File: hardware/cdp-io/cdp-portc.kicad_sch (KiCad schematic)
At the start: 5 parts, among them U1 74LS573, U2 74LS573, U7 74LS00

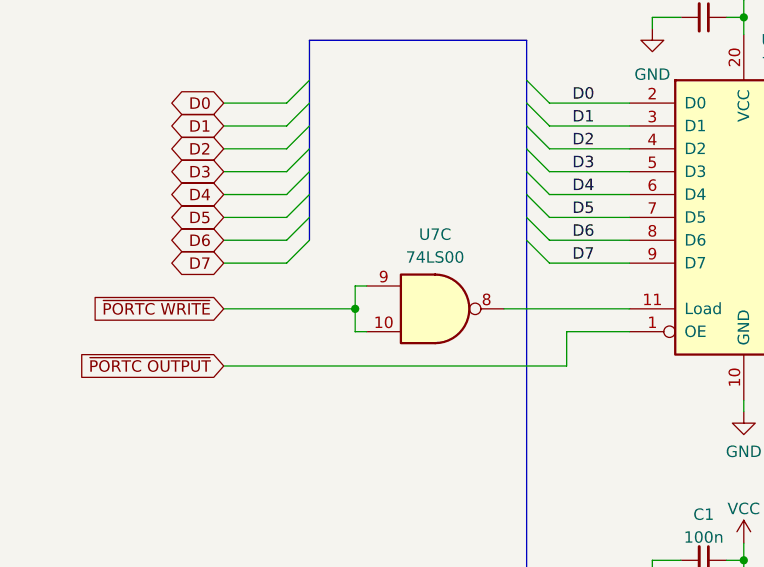
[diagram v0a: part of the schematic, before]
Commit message: The controller is finished. U7 is changed to a hex inverter.
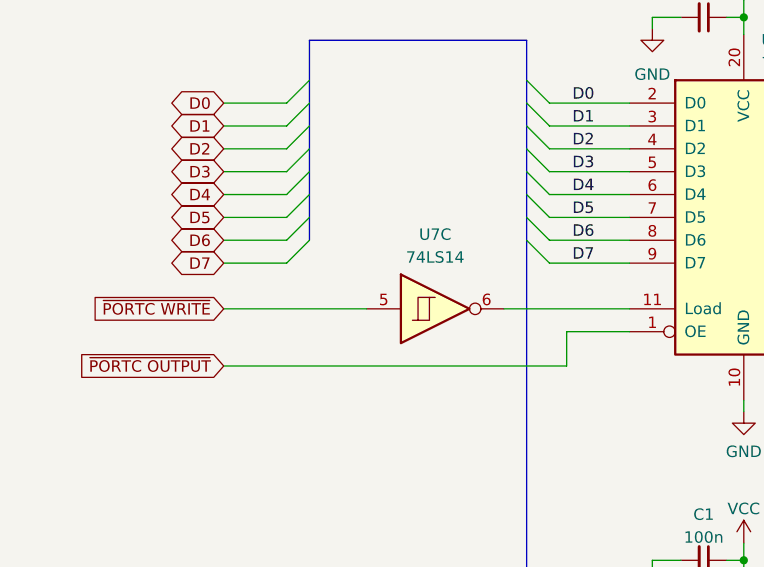
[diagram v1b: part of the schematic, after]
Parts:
- removed U7: 74LS00, symbol 74xx:74LS00
- added U7: 74LS14, symbol 74xx:74LS14
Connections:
- net ~{PORTC WRITE}: now also U7.5
- net at U1.11 (Load): now also U7.6
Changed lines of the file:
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@@
   (junction (at 155.575 33.02) (diameter 0) (color 0 0 0 0)
   )
-  (junction (at 112.395 65.405) (diameter 0) (color 0 0 0 0)
-  )
   (bus_entry (at 181.61 118.11) (size -2.54 2.54)
     (stroke (width 0) (type default))
@@
     (stroke (width 0) (type default))
   )
-  (wire (pts (xy 113.665 62.865) (xy 112.395 62.865))
-    (stroke (width 0) (type default))
-  )
   (wire (pts (xy 133.985 102.87) (xy 142.875 102.87))
     (stroke (width 0) (type default))
@@
     (stroke (width 0) (type default))
   )
-  (wire (pts (xy 112.395 65.405) (xy 112.395 67.945))
-    (stroke (width 0) (type default))
-  )
   (wire (pts (xy 145.415 94.615) (xy 145.415 93.345))
     (stroke (width 0) (type default))
@@
     (stroke (width 0) (type default))
   )
-  (wire (pts (xy 112.395 67.945) (xy 113.665 67.945))
-    (stroke (width 0) (type default))
-  )
   (wire (pts (xy 208.915 60.325) (xy 216.535 60.325))
     (stroke (width 0) (type default))
@@
     (stroke (width 0) (type default))
   )
-  (wire (pts (xy 97.79 65.405) (xy 112.395 65.405))
-    (stroke (width 0) (type default))
-  )
   (bus (pts (xy 206.375 47.625) (xy 206.375 50.165))
     (stroke (width 0) (type default))
@@
     (stroke (width 0) (type default))
   )
+  (wire (pts (xy 97.79 65.405) (xy 113.665 65.405))
+    (stroke (width 0) (type default))
+  )
   (bus (pts (xy 131.445 50.165) (xy 131.445 47.625))
     (stroke (width 0) (type default))
@@
   )
   (wire (pts (xy 145.415 34.29) (xy 145.415 33.02))
-    (stroke (width 0) (type default))
-  )
-  (wire (pts (xy 112.395 62.865) (xy 112.395 65.405))
     (stroke (width 0) (type default))
   )
@@
         (path "/479e9a3e-8705-41df-8009-7e8503809f49/03dab4a8-d44b-4cf8-b119-6efcff8953b4"
           (reference "#PWR018") (unit 1)
+        )
+      )
+    )
+  )
+  (symbol (lib_id "74xx:74LS14") (at 121.285 65.405 0) (unit 3)
+    (in_bom yes) (on_board yes) (dnp no) (fields_autoplaced)
+    (property "Reference" "U7" (at 121.285 57.15 0)
+      (effects (font (size 1.27 1.27)))
+    )
+    (property "Value" "74LS14" (at 121.285 59.69 0)
+      (effects (font (size 1.27 1.27)))
+    )
+    (property "Footprint" "" (at 121.285 65.405 0)
+      (effects (font (size 1.27 1.27)) hide)
+    )
+    (property "Datasheet" "http://www.ti.com/lit/gpn/sn74LS14" (at 121.285 65.405 0)
+      (effects (font (size 1.27 1.27)) hide)
+    )
+    (pin "1")
+    (pin "2")
+    (pin "3")
+    (pin "4")
+    (pin "5")
+    (pin "6")
+    (pin "8")
+    (pin "9")
+    (pin "10")
+    (pin "11")
+    (pin "12")
+    (pin "13")
+    (pin "14")
+    (pin "7")
+    (instances
+      (project "cdp-io"
+        (path "/479e9a3e-8705-41df-8009-7e8503809f49/fc5dd19a-450f-4ce7-af21-025e7154e993"
+          (reference "U7") (unit 3)
+        )
+        (path "/479e9a3e-8705-41df-8009-7e8503809f49/03dab4a8-d44b-4cf8-b119-6efcff8953b4"
+          (reference "U7") (unit 3)
         )
       )
@@
         )
       )
-    )
-  )
-  (symbol (lib_id "74xx:74LS00") (at 121.285 65.405 0) (unit 3)
-    (in_bom yes) (on_board yes) (dnp no) (fields_autoplaced)
-    (property "Reference" "U7" (at 121.2767 57.15 0)
-      (effects (font (size 1.27 1.27)))
-    )
-    (property "Value" "74LS00" (at 121.2767 59.69 0)
-      (effects (font (size 1.27 1.27)))
-    )
-    (property "Footprint" "" (at 121.285 65.405 0)
-      (effects (font (size 1.27 1.27)) hide)
-    )
-    (property "Datasheet" "http://www.ti.com/lit/gpn/sn74ls00" (at 121.285 65.405 0)
-      (effects (font (size 1.27 1.27)) hide)
-    )
-    (pin "1")
-    (pin "2")
-    (pin "3")
-    (pin "4")
-    (pin "5")
-    (pin "6")
-    (pin "10")
-    (pin "8")
-    (pin "9")
-    (pin "11")
-    (pin "12")
-    (pin "13")
-    (pin "14")
-    (pin "7")
-    (instances
-      (project "cdp-io"
-        (path "/479e9a3e-8705-41df-8009-7e8503809f49/03dab4a8-d44b-4cf8-b119-6efcff8953b4"
-          (reference "U7") (unit 3)
-        )
-      )

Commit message: Changed the layout a bit, started to work on the PCB.
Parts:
- U7: footprint (none) -> Package_DIP:DIP-14_W7.62mm_Socket
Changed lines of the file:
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@@
       (effects (font (size 1.27 1.27)))
     )
-    (property "Footprint" "" (at 121.285 65.405 0)
+    (property "Footprint" "Package_DIP:DIP-14_W7.62mm_Socket" (at 121.285 65.405 0)
       (effects (font (size 1.27 1.27)) hide)
     )

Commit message: Changed the schematic a bit.
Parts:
- removed U7: 74LS14, Package_DIP:DIP-14_W7.62mm_Socket, symbol 74xx:74LS14
- added U7: 74LS14, Package_DIP:DIP-14_W7.62mm_Socket, symbol 74xx:74LS14
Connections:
- net ~{PORTC WRITE}: now also U7.9
- net at U1.11 (Load): now also U7.8

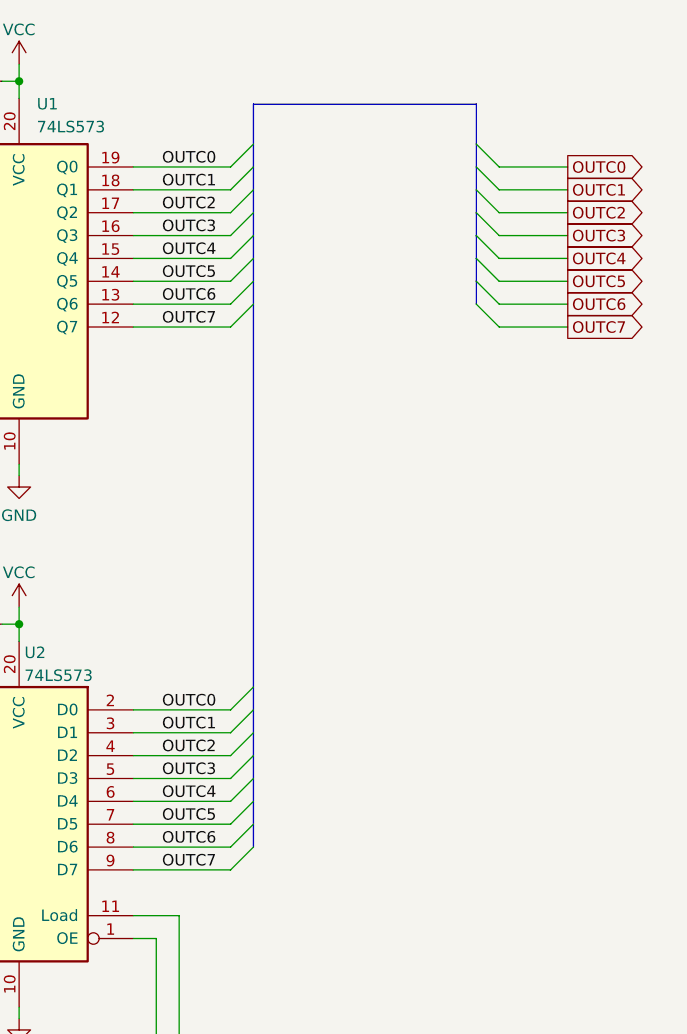
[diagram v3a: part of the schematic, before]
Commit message: Renamed a few net, and changed the schematic a bit. The PCB is ready!
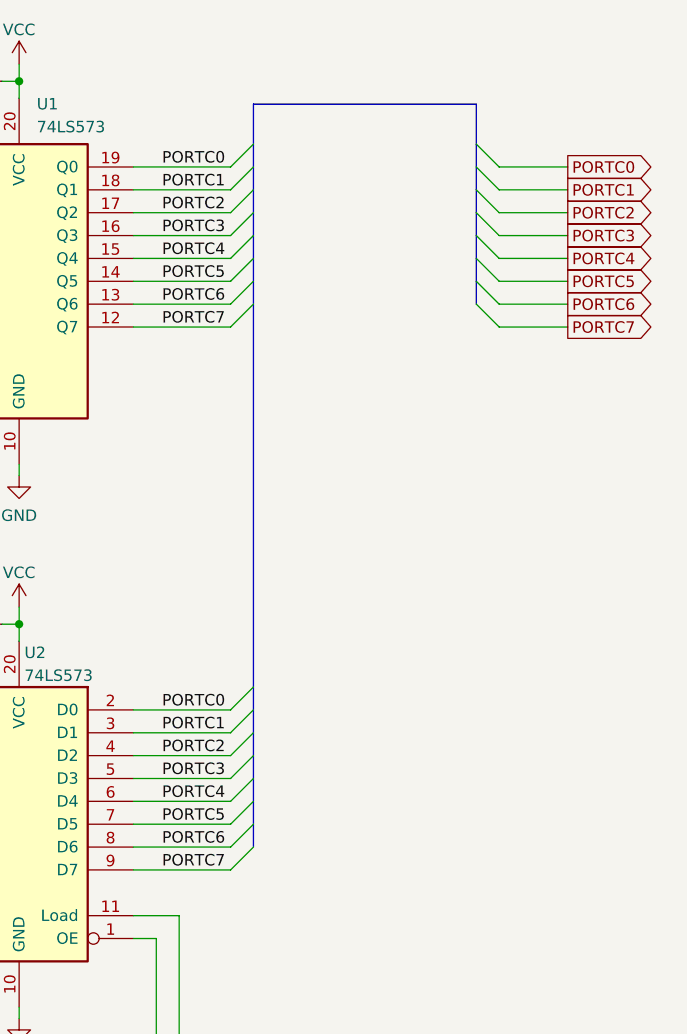
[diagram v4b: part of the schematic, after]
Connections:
- net OUTC0 renamed PORTC0
- net OUTC1 renamed PORTC1
- net OUTC2 renamed PORTC2
- net OUTC3 renamed PORTC3
- net OUTC4 renamed PORTC4
- net OUTC5 renamed PORTC5
- net OUTC6 renamed PORTC6
- net OUTC7 renamed PORTC7
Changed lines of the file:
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@@
     (effects (font (size 1.27 1.27)) (justify left bottom))
   )
-  (label "OUTC7" (at 171.45 120.65 0) (fields_autoplaced)
+  (label "PORTC7" (at 171.45 120.65 0) (fields_autoplaced)
     (effects (font (size 1.27 1.27)) (justify left bottom))
   )
-  (label "OUTC2" (at 171.45 107.95 0) (fields_autoplaced)
+  (label "PORTC2" (at 171.45 107.95 0) (fields_autoplaced)
     (effects (font (size 1.27 1.27)) (justify left bottom))
   )
-  (label "OUTC1" (at 171.45 105.41 0) (fields_autoplaced)
+  (label "PORTC1" (at 171.45 105.41 0) (fields_autoplaced)
     (effects (font (size 1.27 1.27)) (justify left bottom))
   )
@@
     (effects (font (size 1.27 1.27)) (justify left bottom))
   )
-  (label "OUTC5" (at 171.45 115.57 0) (fields_autoplaced)
+  (label "PORTC5" (at 171.45 115.57 0) (fields_autoplaced)
     (effects (font (size 1.27 1.27)) (justify left bottom))
   )
-  (label "OUTC6" (at 171.45 57.785 0) (fields_autoplaced)
+  (label "PORTC6" (at 171.45 57.785 0) (fields_autoplaced)
     (effects (font (size 1.27 1.27)) (justify left bottom))
   )
-  (label "OUTC3" (at 171.45 50.165 0) (fields_autoplaced)
+  (label "PORTC3" (at 171.45 50.165 0) (fields_autoplaced)
     (effects (font (size 1.27 1.27)) (justify left bottom))
   )
-  (label "OUTC0" (at 171.45 102.87 0) (fields_autoplaced)
+  (label "PORTC0" (at 171.45 102.87 0) (fields_autoplaced)
     (effects (font (size 1.27 1.27)) (justify left bottom))
   )
-  (label "OUTC7" (at 171.45 60.325 0) (fields_autoplaced)
+  (label "PORTC7" (at 171.45 60.325 0) (fields_autoplaced)
     (effects (font (size 1.27 1.27)) (justify left bottom))
   )
@@
     (effects (font (size 1.27 1.27)) (justify left bottom))
   )
-  (label "OUTC5" (at 171.45 55.245 0) (fields_autoplaced)
+  (label "PORTC5" (at 171.45 55.245 0) (fields_autoplaced)
     (effects (font (size 1.27 1.27)) (justify left bottom))
   )
-  (label "OUTC3" (at 171.45 110.49 0) (fields_autoplaced)
+  (label "PORTC3" (at 171.45 110.49 0) (fields_autoplaced)
     (effects (font (size 1.27 1.27)) (justify left bottom))
   )
-  (label "OUTC4" (at 171.45 52.705 0) (fields_autoplaced)
+  (label "PORTC4" (at 171.45 52.705 0) (fields_autoplaced)
     (effects (font (size 1.27 1.27)) (justify left bottom))
   )
-  (label "OUTC6" (at 171.45 118.11 0) (fields_autoplaced)
+  (label "PORTC6" (at 171.45 118.11 0) (fields_autoplaced)
     (effects (font (size 1.27 1.27)) (justify left bottom))
   )
-  (label "OUTC1" (at 171.45 45.085 0) (fields_autoplaced)
+  (label "PORTC1" (at 171.45 45.085 0) (fields_autoplaced)
     (effects (font (size 1.27 1.27)) (justify left bottom))
   )
@@
     (effects (font (size 1.27 1.27)) (justify left bottom))
   )
-  (label "OUTC0" (at 171.45 42.545 0) (fields_autoplaced)
+  (label "PORTC0" (at 171.45 42.545 0) (fields_autoplaced)
     (effects (font (size 1.27 1.27)) (justify left bottom))
   )
@@
     (effects (font (size 1.27 1.27)) (justify left bottom))
   )
-  (label "OUTC2" (at 171.45 47.625 0) (fields_autoplaced)
+  (label "PORTC2" (at 171.45 47.625 0) (fields_autoplaced)
     (effects (font (size 1.27 1.27)) (justify left bottom))
   )
@@
     (effects (font (size 1.27 1.27)) (justify left bottom))
   )
-  (label "OUTC4" (at 171.45 113.03 0) (fields_autoplaced)
+  (label "PORTC4" (at 171.45 113.03 0) (fields_autoplaced)
     (effects (font (size 1.27 1.27)) (justify left bottom))
   )
@@
     )
   )
-  (global_label "OUTC1" (shape output) (at 216.535 45.085 0) (fields_autoplaced)
+  (global_label "PORTC1" (shape output) (at 216.535 45.085 0) (fields_autoplaced)
     (effects (font (size 1.27 1.27)) (justify left))
-    (property "Intersheetrefs" "${INTERSHEET_REFS}" (at 225.5489 45.085 0)
+    (property "Intersheetrefs" "${INTERSHEET_REFS}" (at 226.7584 45.085 0)
       (effects (font (size 1.27 1.27)) (justify left) hide)
     )
   )
-  (global_label "OUTC2" (shape output) (at 216.535 47.625 0) (fields_autoplaced)
+  (global_label "PORTC2" (shape output) (at 216.535 47.625 0) (fields_autoplaced)
     (effects (font (size 1.27 1.27)) (justify left))
-    (property "Intersheetrefs" "${INTERSHEET_REFS}" (at 225.5489 47.625 0)
+    (property "Intersheetrefs" "${INTERSHEET_REFS}" (at 226.7584 47.625 0)
       (effects (font (size 1.27 1.27)) (justify left) hide)
     )
   )
-  (global_label "OUTC0" (shape output) (at 216.535 42.545 0) (fields_autoplaced)
+  (global_label "PORTC0" (shape output) (at 216.535 42.545 0) (fields_autoplaced)
     (effects (font (size 1.27 1.27)) (justify left))
-    (property "Intersheetrefs" "${INTERSHEET_REFS}" (at 225.5489 42.545 0)
+    (property "Intersheetrefs" "${INTERSHEET_REFS}" (at 226.7584 42.545 0)
       (effects (font (size 1.27 1.27)) (justify left) hide)
     )
   )
-  (global_label "OUTC7" (shape output) (at 216.535 60.325 0) (fields_autoplaced)
+  (global_label "PORTC7" (shape output) (at 216.535 60.325 0) (fields_autoplaced)
     (effects (font (size 1.27 1.27)) (justify left))
-    (property "Intersheetrefs" "${INTERSHEET_REFS}" (at 225.5489 60.325 0)
+    (property "Intersheetrefs" "${INTERSHEET_REFS}" (at 226.7584 60.325 0)
       (effects (font (size 1.27 1.27)) (justify left) hide)
     )
   )
-  (global_label "OUTC4" (shape output) (at 216.535 52.705 0) (fields_autoplaced)
+  (global_label "PORTC4" (shape output) (at 216.535 52.705 0) (fields_autoplaced)
     (effects (font (size 1.27 1.27)) (justify left))
-    (property "Intersheetrefs" "${INTERSHEET_REFS}" (at 225.5489 52.705 0)
+    (property "Intersheetrefs" "${INTERSHEET_REFS}" (at 226.7584 52.705 0)
       (effects (font (size 1.27 1.27)) (justify left) hide)
     )
@@
     )
   )
-  (global_label "OUTC5" (shape output) (at 216.535 55.245 0) (fields_autoplaced)
+  (global_label "PORTC5" (shape output) (at 216.535 55.245 0) (fields_autoplaced)
     (effects (font (size 1.27 1.27)) (justify left))
-    (property "Intersheetrefs" "${INTERSHEET_REFS}" (at 225.5489 55.245 0)
+    (property "Intersheetrefs" "${INTERSHEET_REFS}" (at 226.7584 55.245 0)
       (effects (font (size 1.27 1.27)) (justify left) hide)
     )
@@
     )
   )
-  (global_label "OUTC3" (shape output) (at 216.535 50.165 0) (fields_autoplaced)
+  (global_label "PORTC3" (shape output) (at 216.535 50.165 0) (fields_autoplaced)
     (effects (font (size 1.27 1.27)) (justify left))
-    (property "Intersheetrefs" "${INTERSHEET_REFS}" (at 225.5489 50.165 0)
+    (property "Intersheetrefs" "${INTERSHEET_REFS}" (at 226.7584 50.165 0)
       (effects (font (size 1.27 1.27)) (justify left) hide)
     )
   )
-  (global_label "OUTC6" (shape output) (at 216.535 57.785 0) (fields_autoplaced)
+  (global_label "PORTC6" (shape output) (at 216.535 57.785 0) (fields_autoplaced)
     (effects (font (size 1.27 1.27)) (justify left))
-    (property "Intersheetrefs" "${INTERSHEET_REFS}" (at 225.5489 57.785 0)
+    (property "Intersheetrefs" "${INTERSHEET_REFS}" (at 226.7584 57.785 0)
       (effects (font (size 1.27 1.27)) (justify left) hide)
     )

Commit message: The final version of the IO board. Gerber files added.
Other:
- company: (none) -> ZLED
- title: (none) -> Port C
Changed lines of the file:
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@@
 (kicad_sch (version 20230121) (generator eeschema)
   (paper "A4")
+  (title_block
+    (title "Port C")
+    (date "2023-07-06")
+    (rev "1")
+    (company "ZLED")
+  )
   (junction (at 155.575 93.345) (diameter 0) (color 0 0 0 0)
   )

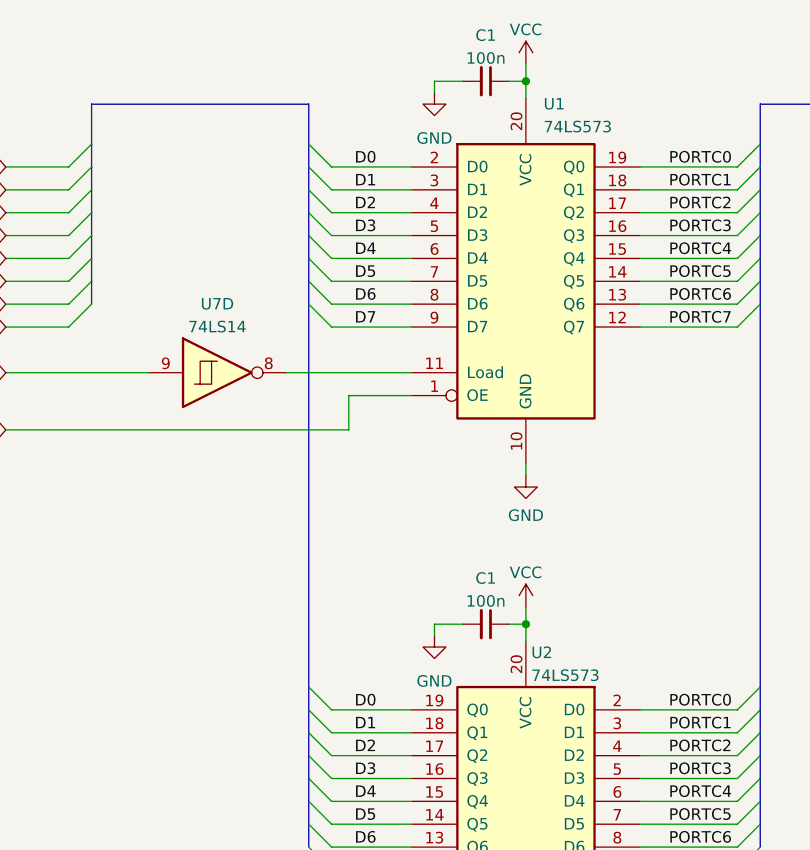
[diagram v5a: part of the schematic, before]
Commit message: IC names fixed. PCB is updated. Gerber files are still ok.
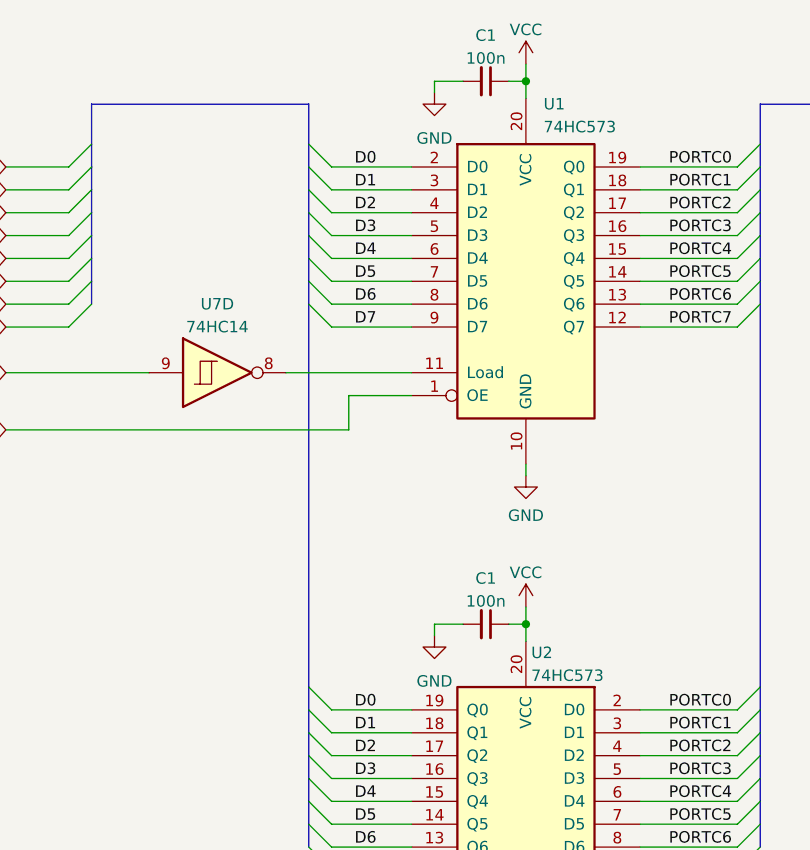
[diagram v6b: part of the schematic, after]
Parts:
- U1, U2: value 74LS573 -> 74HC573
- U7: value 74LS14 -> 74HC14
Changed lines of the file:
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@@
       (effects (font (size 1.27 1.27)))
     )
-    (property "Value" "74LS14" (at 121.285 60.325 0)
+    (property "Value" "74HC14" (at 121.285 60.325 0)
       (effects (font (size 1.27 1.27)))
     )
@@
       (effects (font (size 1.27 1.27)) (justify right))
     )
-    (property "Value" "74LS573" (at 156.1591 99.06 0)
+    (property "Value" "74HC573" (at 156.1591 99.06 0)
       (effects (font (size 1.27 1.27)) (justify right))
     )
@@
       (effects (font (size 1.27 1.27)) (justify left))
     )
-    (property "Value" "74LS573" (at 157.5309 38.1 0)
+    (property "Value" "74HC573" (at 157.5309 38.1 0)
       (effects (font (size 1.27 1.27)) (justify left))
     )
